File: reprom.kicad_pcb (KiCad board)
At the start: 2 copper layers, 43.2 x 43.2 mm, 14 parts, among them P1 KERNAL_SOCKET, P2 KERNAL_AND_BASIC_SOCKET, P3 LEFT_SOCKET, P4 RIGHT_SOCKET, P5 KERNAL, P6 CHARSET, P7 BASIC, U1 27512, U2 GAL16V8

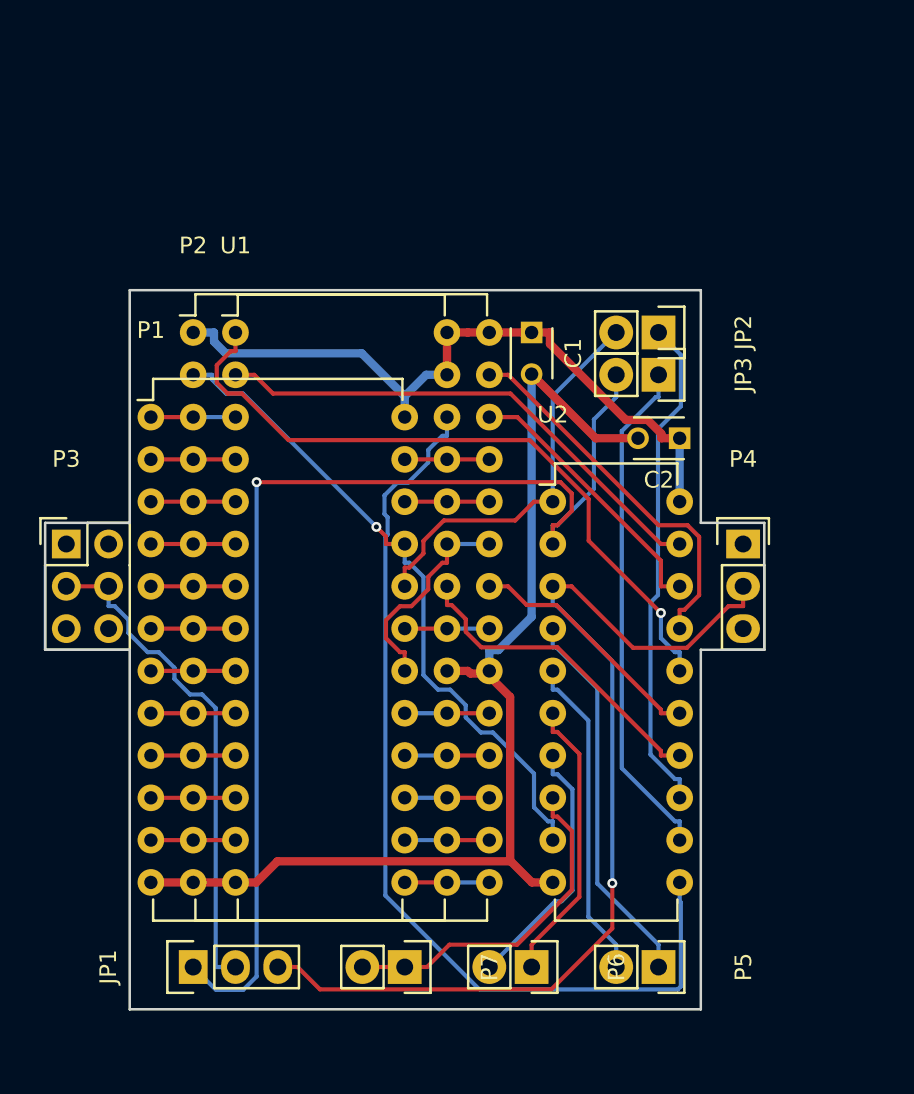
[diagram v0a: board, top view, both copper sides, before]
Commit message: Hardware: Removed crappy autorouting, improved part placement
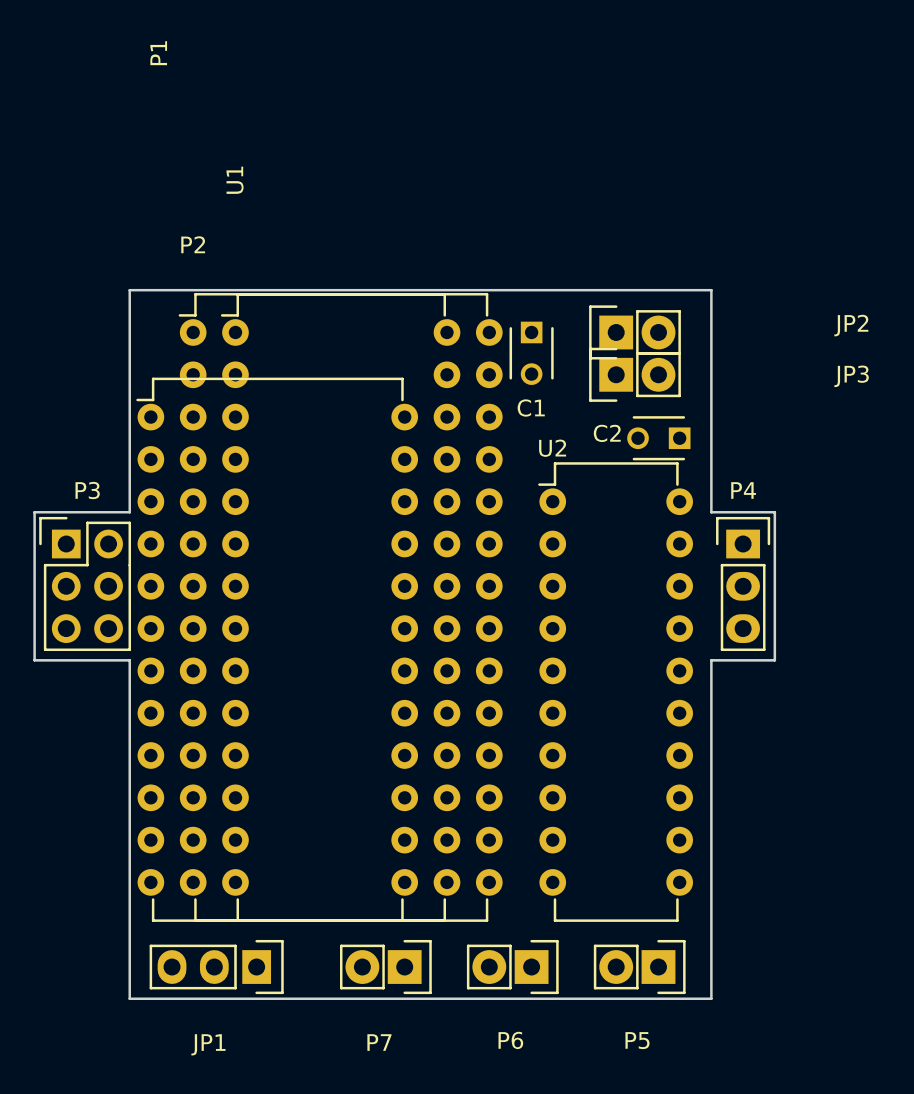
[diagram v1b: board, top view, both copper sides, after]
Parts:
- moved JP1 3.81 mm to (54.6, 99.1), turned to 270 degrees
- moved JP2 2.54 mm to (76.2, 61.0), turned to 90 degrees
- moved JP3 2.54 mm to (76.2, 63.5), turned to 90 degrees
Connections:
- JP1 pad 1: /BS -> /CS
- JP1 pad 3: /CS -> /BS
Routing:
- net /BS: track 69.2 -> 0.00 mm, vias 1 -> 0
- net GND: track 66.9 -> 0.00 mm
- net /CS: track 59.5 -> 0.00 mm, vias 1 -> 0
- net /BA14: track 57.4 -> 0.00 mm
- net VCC: track 42.4 -> 0.00 mm
- net /A15: track 41.6 -> 0.00 mm, vias 1 -> 0
- net /BA12: track 40.0 -> 0.00 mm, vias 1 -> 0
- net /A12: track 30.9 -> 0.00 mm
- net /CBS: track 30.6 -> 0.00 mm
- net /BCS: track 30.3 -> 0.00 mm
- net /CKS: track 30.1 -> 0.00 mm
- net /KS: track 23.8 -> 0.00 mm
- net /K0: track 23.1 -> 0.00 mm
- net /A14: track 22.8 -> 0.00 mm
- net /B0: track 20.7 -> 0.00 mm
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- removed copper zone on B.Cu, net GND
- removed copper zone on F.Cu, net GND
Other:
- board size 43.2 x 43.2 mm -> 44.4 x 42.5 mm

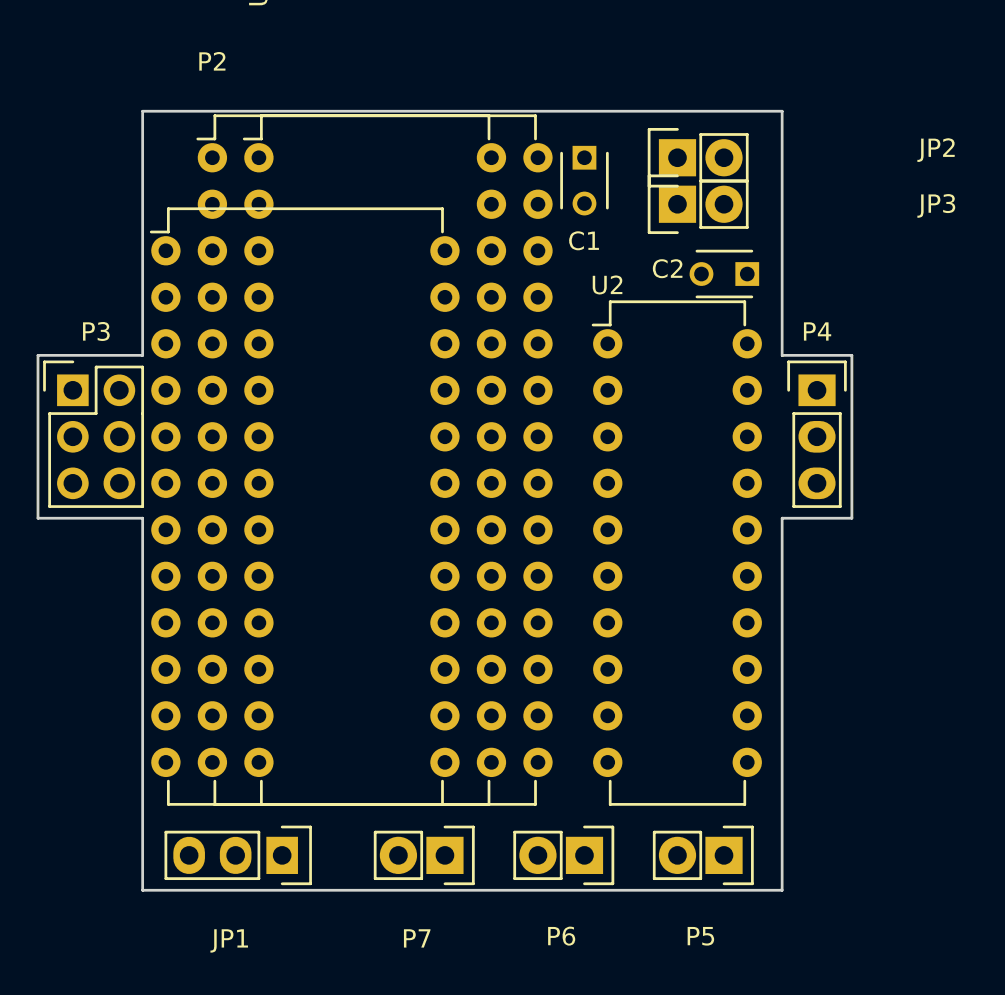
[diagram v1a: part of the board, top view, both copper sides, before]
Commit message: Hardware: Some initial routing
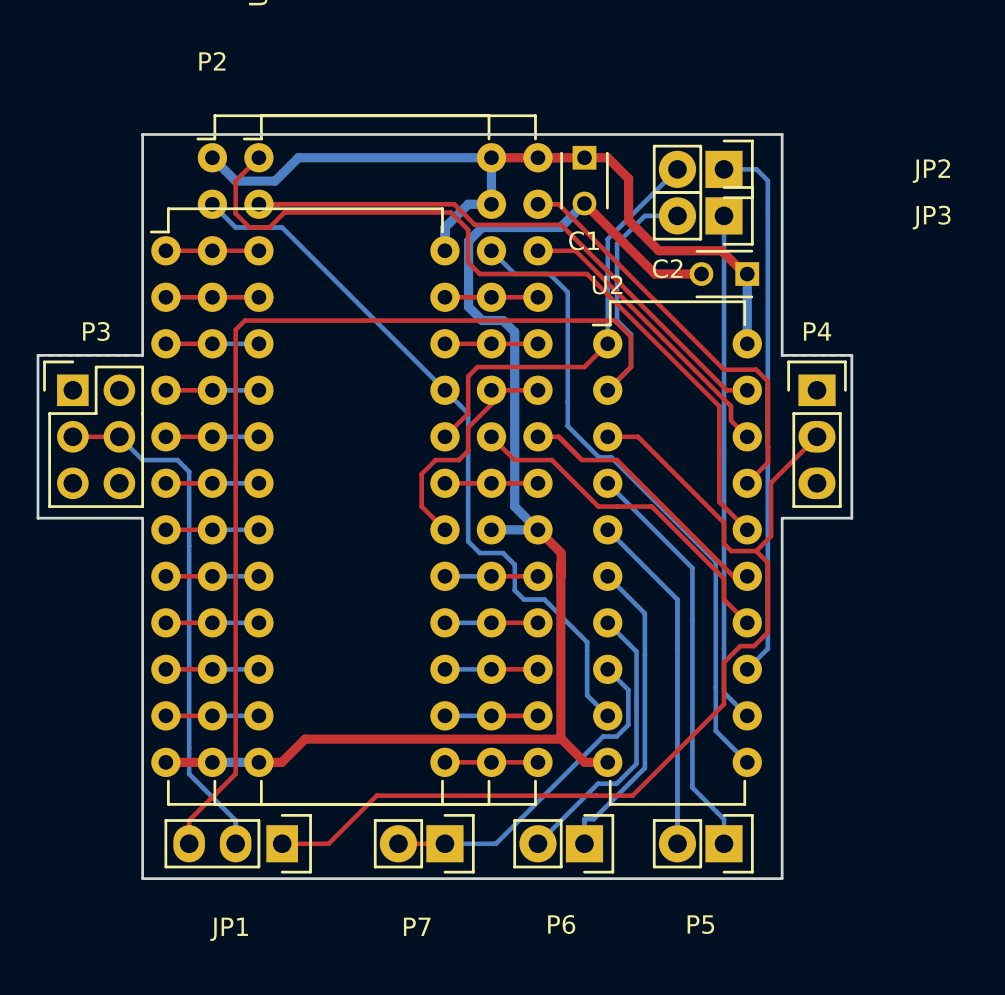
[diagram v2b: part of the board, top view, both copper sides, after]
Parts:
- moved JP3 2.62 mm to (78.7, 64.1), turned to 270 degrees
- moved JP2 2.62 mm to (78.7, 61.6), turned to 270 degrees
- moved JP1 0.64 mm to (54.6, 98.4)
- moved P5 0.64 mm to (78.7, 98.4)
- moved P6 0.64 mm to (71.1, 98.4)
- moved P7 0.64 mm to (63.5, 98.4)
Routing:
- net GND: track 0.00 -> 73.5 mm
- net /BS: track 0.00 -> 67.6 mm
- net /CS: track 0.00 -> 56.5 mm
- net VCC: track 0.00 -> 47.4 mm
- net /A15: track 0.00 -> 43.4 mm
- net /BA12: track 0.00 -> 39.8 mm
- net /BA14: track 0.00 -> 35.2 mm
- net /A12: track 0.00 -> 32.0 mm
- net /CKS: track 0.00 -> 29.8 mm
- net /BCS: track 0.00 -> 28.5 mm
- net /CBS: track 0.00 -> 27.8 mm
- net /KS: track 0.00 -> 23.3 mm
- net /A14: track 0.00 -> 22.6 mm
- net /K0: track 0.00 -> 22.3 mm
- net /KBS: track 0.00 -> 18.8 mm
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- added copper zone on B.Cu, net GND
- added copper zone on F.Cu, net GND
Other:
- board size 44.4 x 42.5 mm -> 44.4 x 40.6 mm

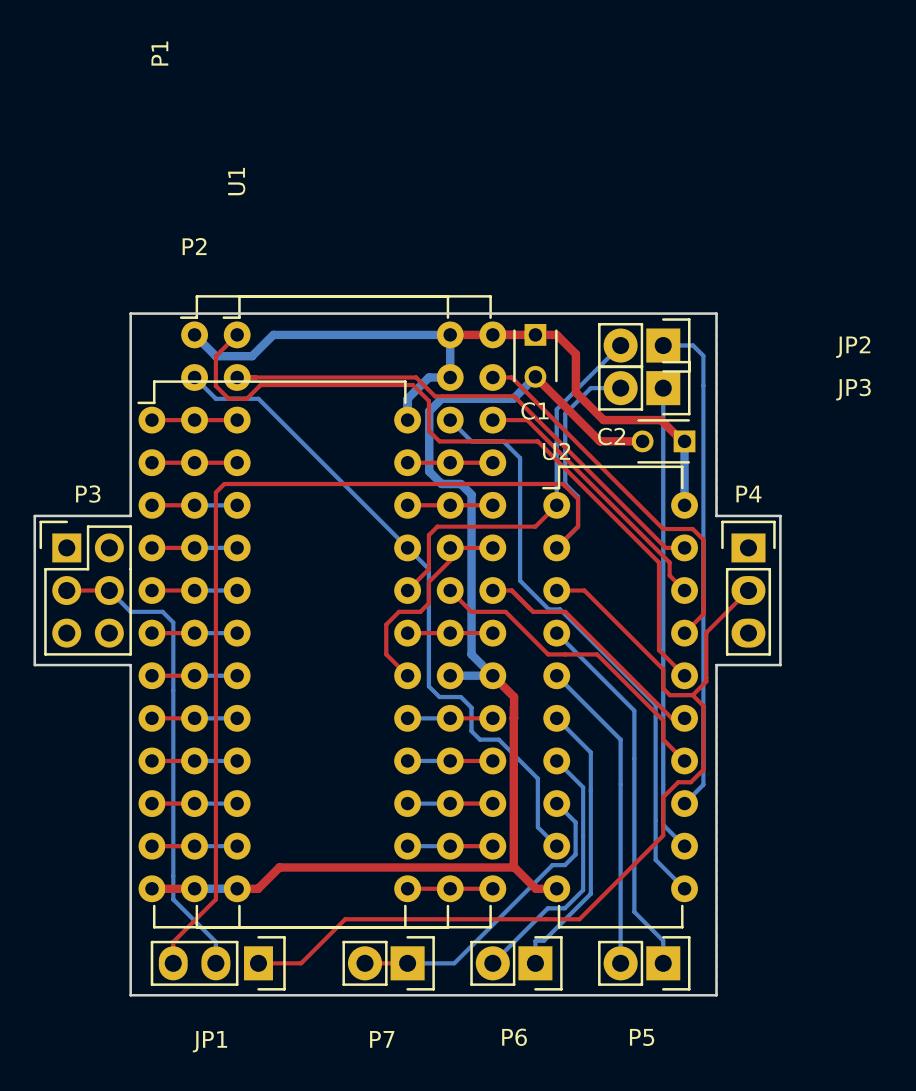
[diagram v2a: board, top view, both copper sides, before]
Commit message: Hardware: Improved routing, designed silkscreen, improved schematics
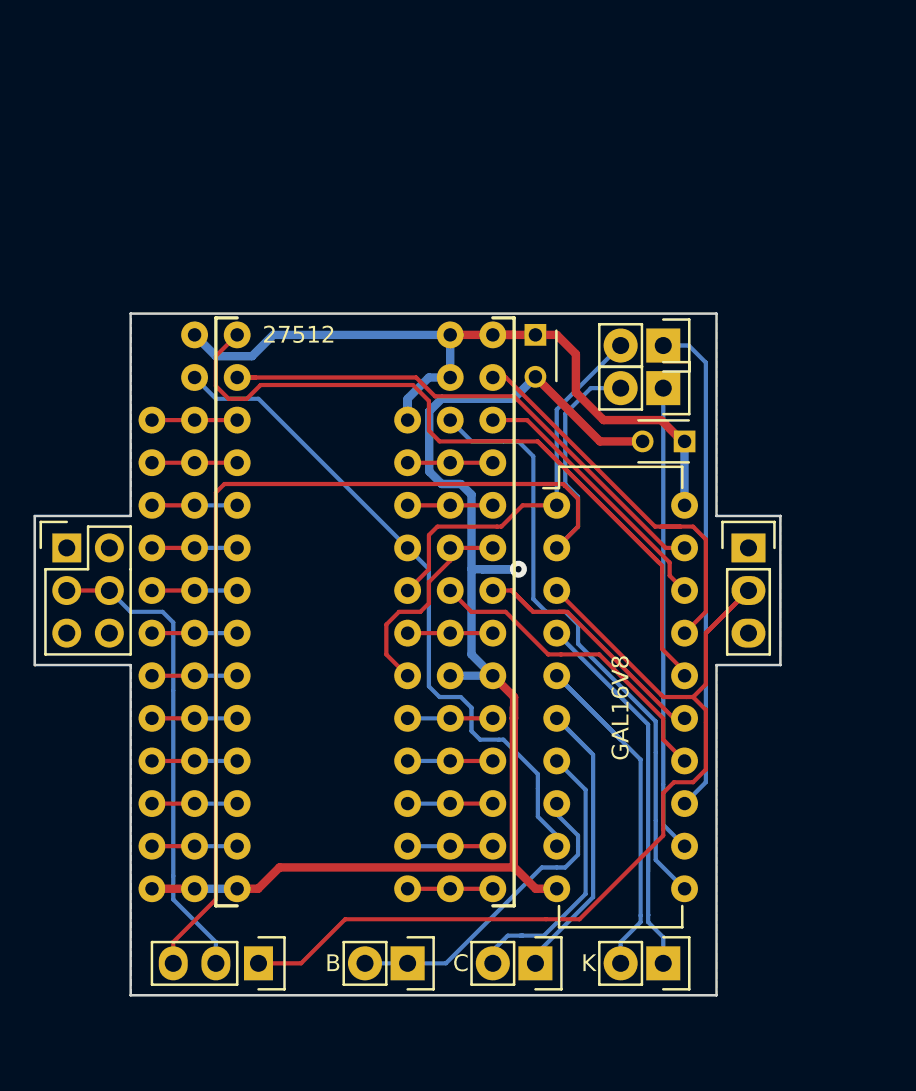
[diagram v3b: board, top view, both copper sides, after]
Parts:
- P1: footprint Housings_DIP:DIP-24_W15.24mm -> custom:DIP-24_W15.24mm
- P2, U1: footprint Housings_DIP:DIP-28_W15.24mm -> custom:DIP-28_W15.24mm
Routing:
- net /A15: track 43.4 -> 54.1 mm
- net /K1: track 18.7 -> 26.2 mm
- net GND: track 73.5 -> 78.5 mm, vias 0 -> 1
- net /C0: track 17.1 -> 21.5 mm
- net /CS: track 56.5 -> 59.7 mm
- net /K0: track 22.3 -> 23.7 mm
- net /A14: track 22.6 -> 24.0 mm
- net /C1: track 15.5 -> 16.5 mm
- net /BA14: track 35.2 -> 36.0 mm
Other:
- net class Default: via_dia 0.6 -> 1.016; via_drill 0.4 -> 0.381
- net class Power: via_dia 0.6 -> 1.016; via_drill 0.4 -> 0.381
- board text added: "B"
- board text added: "C"
- board text added: "K"

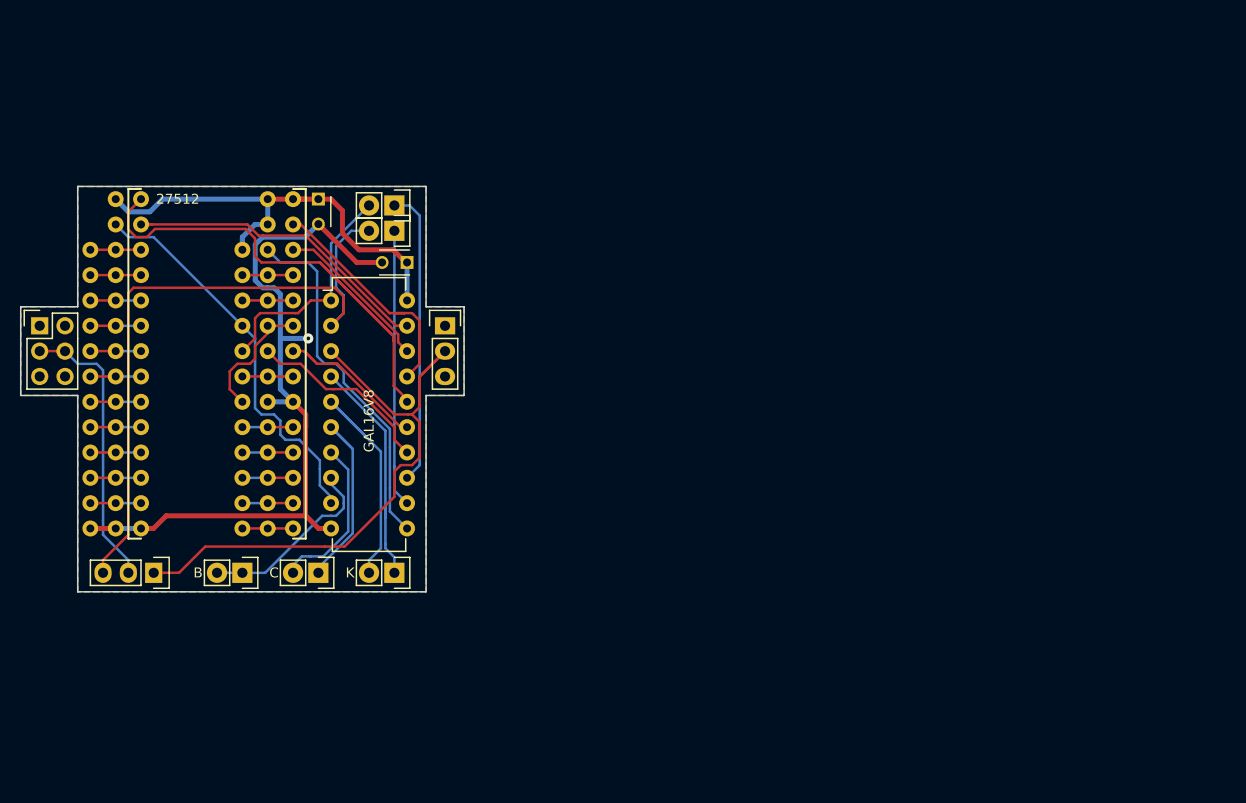
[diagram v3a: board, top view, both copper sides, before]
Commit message: Hardware: Improved routing
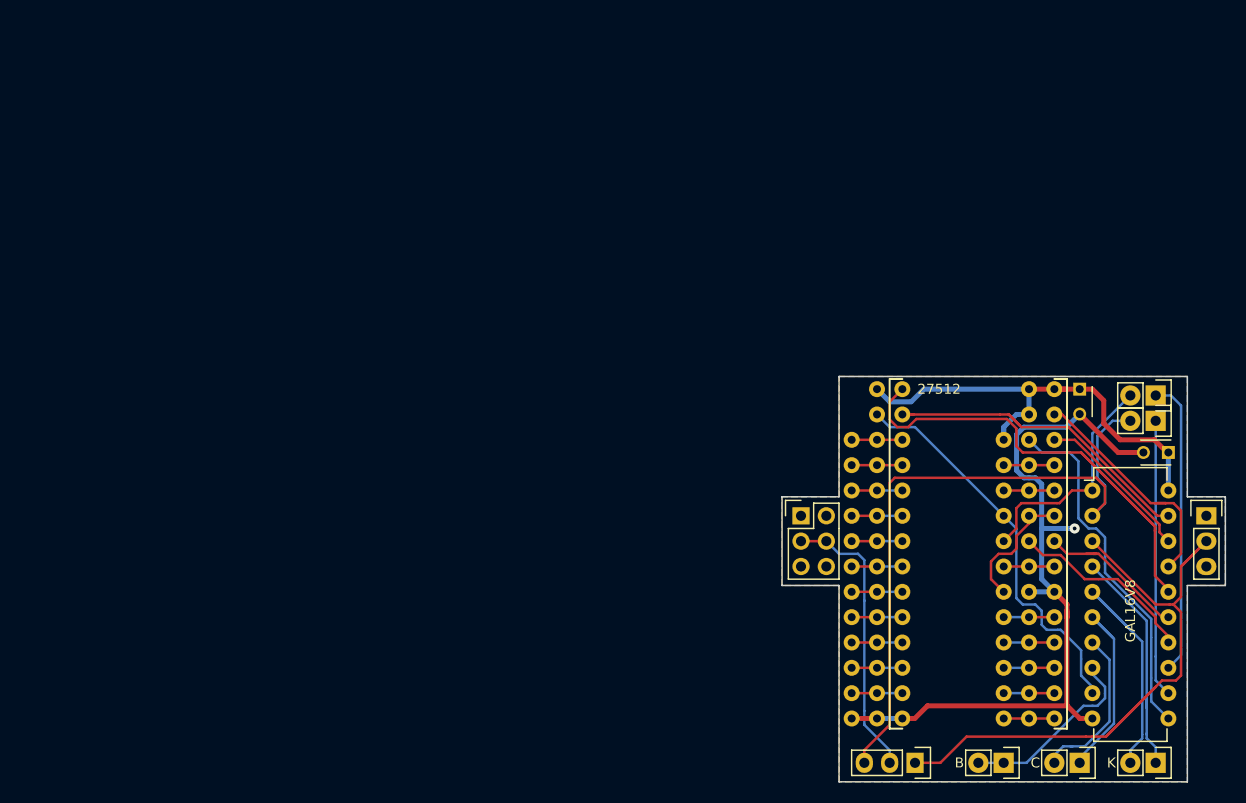
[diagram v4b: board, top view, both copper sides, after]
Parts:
- moved JP1 78.7 mm to (130.9, 117.5)
- moved JP2 78.7 mm to (155.1, 80.6)
- moved JP3 78.7 mm to (155.1, 83.2)
- moved P5 78.7 mm to (155.1, 117.5)
- moved U2 78.7 mm to (148.7, 90.2)
- moved C1 78.7 mm to (147.4, 80.0)
- moved P1 78.7 mm to (124.6, 85.1)
- moved P2 78.7 mm to (127.1, 80.0)
- moved P3 78.7 mm to (119.5, 92.7)
- moved P4 78.7 mm to (160.1, 92.7)
- moved P6 78.7 mm to (147.4, 117.5)
- moved P7 78.7 mm to (139.8, 117.5)
- moved U1 78.7 mm to (129.7, 80.0)
- moved C2 78.7 mm to (156.3, 86.4)
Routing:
- net /CS: track 59.7 -> 66.9 mm
- net /A12: track 32.0 -> 33.7 mm
- net GND: track 78.5 -> 79.5 mm
- net /OE: track 16.6 -> 16.0 mm
